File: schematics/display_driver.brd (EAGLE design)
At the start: 100 x 50 mm, 70 parts, among them IC1 TPIC6B595N, IC2 TPIC6B595N, Q1 IRF9530, Q10 BC547A, Q11 IRF9530, Q12 BC547A, Q2 IRF9530, Q3 BC547A, Q4 BC547A, Q5 IRF9530, Q6 BC547A, Q7 IRF9530, Q8 BC547A, Q9 IRF9530

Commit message: schematics: current prototyping status
Working sample :)
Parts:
- removed C_LDP, C_LSDP: (no value), wirepad:1,6/0,9
- removed Q10, Q12, Q3, Q4, Q6, Q8: BC547A, transistor-npn:TO92
- removed R10, R2, R22, R24, R7, R8: 220, resistor:0204/7
- removed R11, R12, R4, R5: 2.2k, resistor:0204/5
- removed R20: 680R, resistor:0207/10
- removed R25, R26: 2.2k, resistor:0207/10
- added BUZZ1: F/BC40, buzzer:F/BC40
- added T1: BC547, transistor:TO92
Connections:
- removed net D7: IC1.17, R20.1
- removed net L_DP: C_LDP.1, C_LSDP.1, R20.2
- removed net N$10: Q7.G, R10.2, R9.1
- removed net N$11: Q8.3, R10.1
- removed net N$13: Q8.2, R4.2
- removed net N$14: Q4.2, R5.2
- removed net N$15: Q6.2, R11.2
- removed net N$16: Q3.2, R12.2
- removed net N$3: Q3.3, R2.1
- removed net N$43: Q9.G, R21.1, R22.2
- removed net N$44: Q10.3, R22.1
- removed net N$45: Q11.G, R23.1, R24.2
- removed net N$46: Q12.3, R24.1
- removed net N$48: Q12.2, R25.2
- removed net N$49: Q10.2, R26.2
- removed net N$5: Q5.G, R6.1, R7.2
- removed net N$6: Q6.3, R7.1
- removed net N$7: Q2.G, R3.1, R8.2
- removed net N$8: Q4.3, R8.1
- new net BUZZ_CTL: CONTROL.6, T1.2
- net +12V: now also BUZZ1.+
- net B_1: now also Q7.G, R9.1; no longer R4.1
- net B_2: now also Q2.G, R3.1; no longer R5.1
- net B_3: now also Q5.G, R6.1; no longer R11.1
- net B_4: now also Q1.G, R1.1; no longer R12.1
- net GND: now also T1.1; no longer Q10.1, Q12.1, Q3.1, Q4.1, Q6.1, Q8.1
- net N$2: now also BUZZ1.-, T1.3; no longer Q1.G, R1.1, R2.2
- net S_1: now also Q11.G, R23.1; no longer R25.1
- net S_2: now also Q9.G, R21.1; no longer R26.1
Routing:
- net BUZZ_CTL: track 0.00 -> 69.2 mm
- net B_3: track 2.54 -> 58.4 mm
- net S_1: track 0.00 -> 55.9 mm
- net GND: track 173.3 -> 118.4 mm, vias 7 -> 6
- net B_4: track 2.54 -> 48.8 mm
- net N$16: track 43.7 -> 0.00 mm
- net N$13: track 42.0 -> 0.00 mm
- net N$14: track 41.1 -> 0.00 mm
- net N$15: track 39.8 -> 0.00 mm
- net B_2: track 2.54 -> 40.2 mm
- net N$48: track 34.9 -> 0.00 mm, vias 1 -> 0
- net B_1: track 2.54 -> 33.0 mm
- net S_2: track 0.00 -> 27.0 mm
- net +12V: track 132.1 -> 156.7 mm
- net N$49: track 14.9 -> 0.00 mm, vias 1 -> 0
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
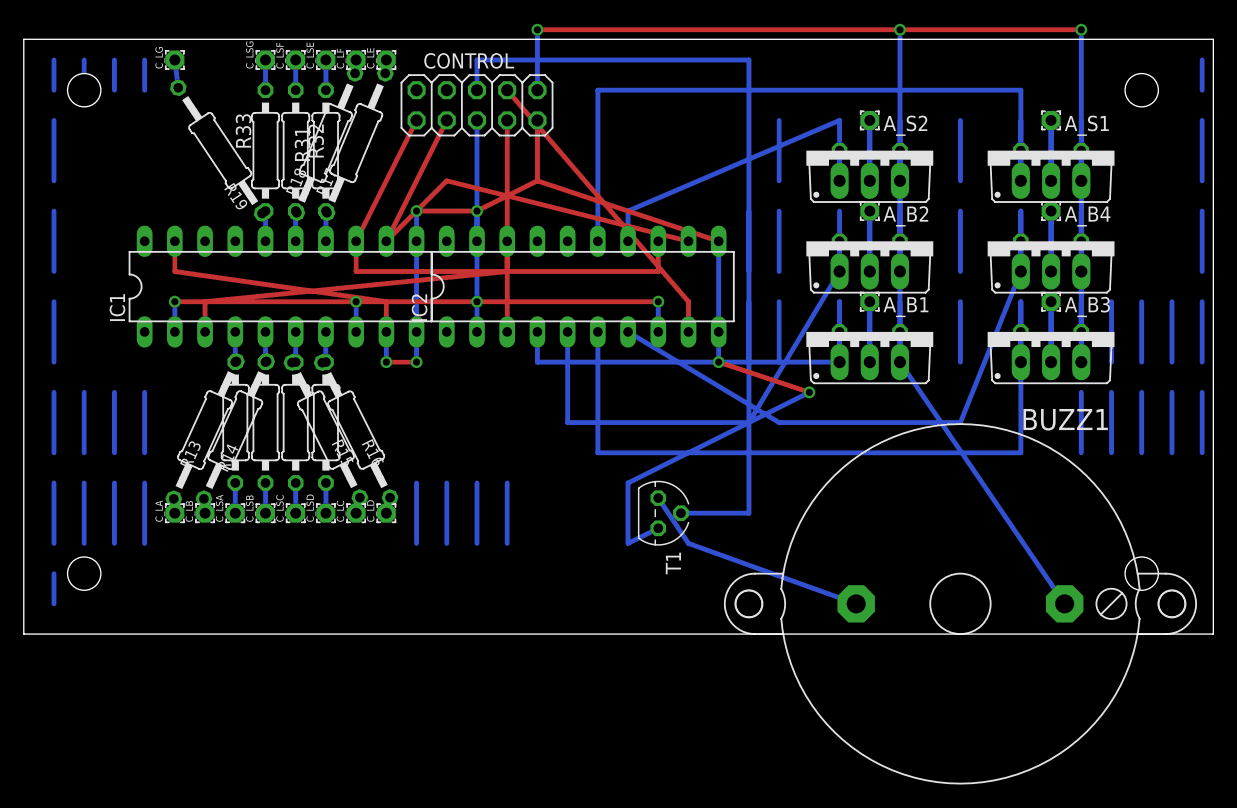
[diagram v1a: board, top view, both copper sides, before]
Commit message: schematics: add correct MOSFET parts, improve redability
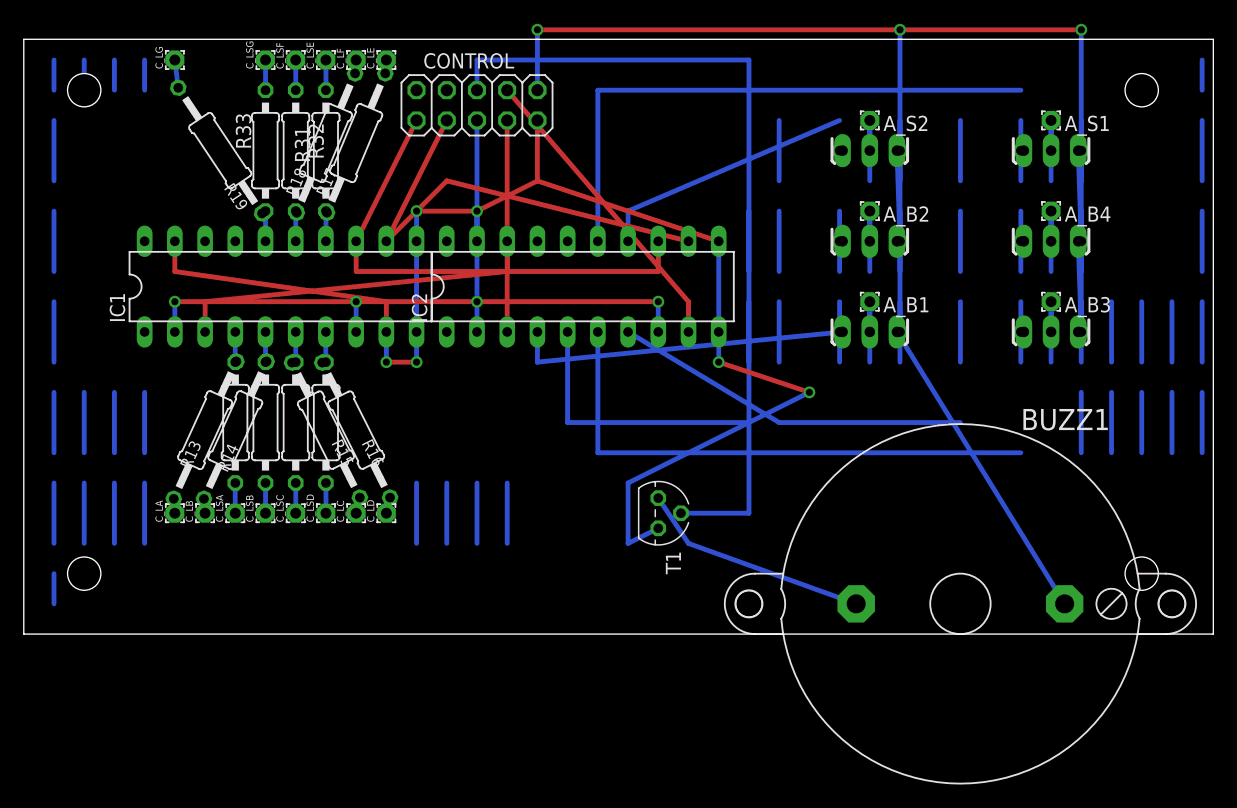
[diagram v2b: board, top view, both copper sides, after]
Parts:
- removed Q11, Q7, Q9: IRF9530, transistor-power:TO220BV
- added Q3, Q4, Q6: IRFU9024V, MINE:TO251AA-V
- Q1, Q2, Q5: value IRF9530 -> IRFU9024V; device transistor-power:TO220BV -> MINE:TO251AA-V
- moved Q1 17.0 mm to (71.1, 25.4)
- moved Q5 15.2 mm to (86.4, 40.6)
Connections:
- net +12V: now also Q1.3, Q2.3, Q3.3, Q4.3, Q5.3, Q6.3; no longer Q1.S, Q11.S, Q2.S, Q5.S, Q7.S, Q9.S
- net B_1: now also Q1.1; no longer Q7.G
- net B_2: now also Q2.1; no longer Q2.G
- net B_3: now also Q3.1; no longer Q5.G
- net B_4: now also Q4.1; no longer Q1.G
- net N$1: now also Q1.2; no longer Q7.D
- net N$12: now also Q4.2; no longer Q1.D
- net N$4: now also Q2.2; no longer Q2.D
- net N$42: now also Q6.2; no longer Q9.D
- net N$47: now also Q5.2; no longer Q11.D
- net N$9: now also Q3.2; no longer Q5.D
- net S_1: now also Q5.1; no longer Q11.G
- net S_2: now also Q6.1; no longer Q9.G
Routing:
- net B_4: track 48.8 -> 30.1 mm
- net B_2: track 40.2 -> 22.9 mm
- net B_3: track 58.4 -> 45.7 mm
- net S_1: track 55.9 -> 48.3 mm
- net S_2: track 27.0 -> 21.9 mm
- net B_1: track 33.0 -> 28.3 mm
- net +12V: track 156.7 -> 152.9 mm
- net N$4: track 5.08 -> 2.54 mm
- net N$12: track 5.08 -> 2.54 mm
- net N$9: track 5.08 -> 2.54 mm
- net N$47: track 5.08 -> 2.54 mm
- net N$42: track 5.08 -> 2.54 mm
- net N$1: track 5.08 -> 2.54 mm

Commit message: schematics: clean up, new design rules
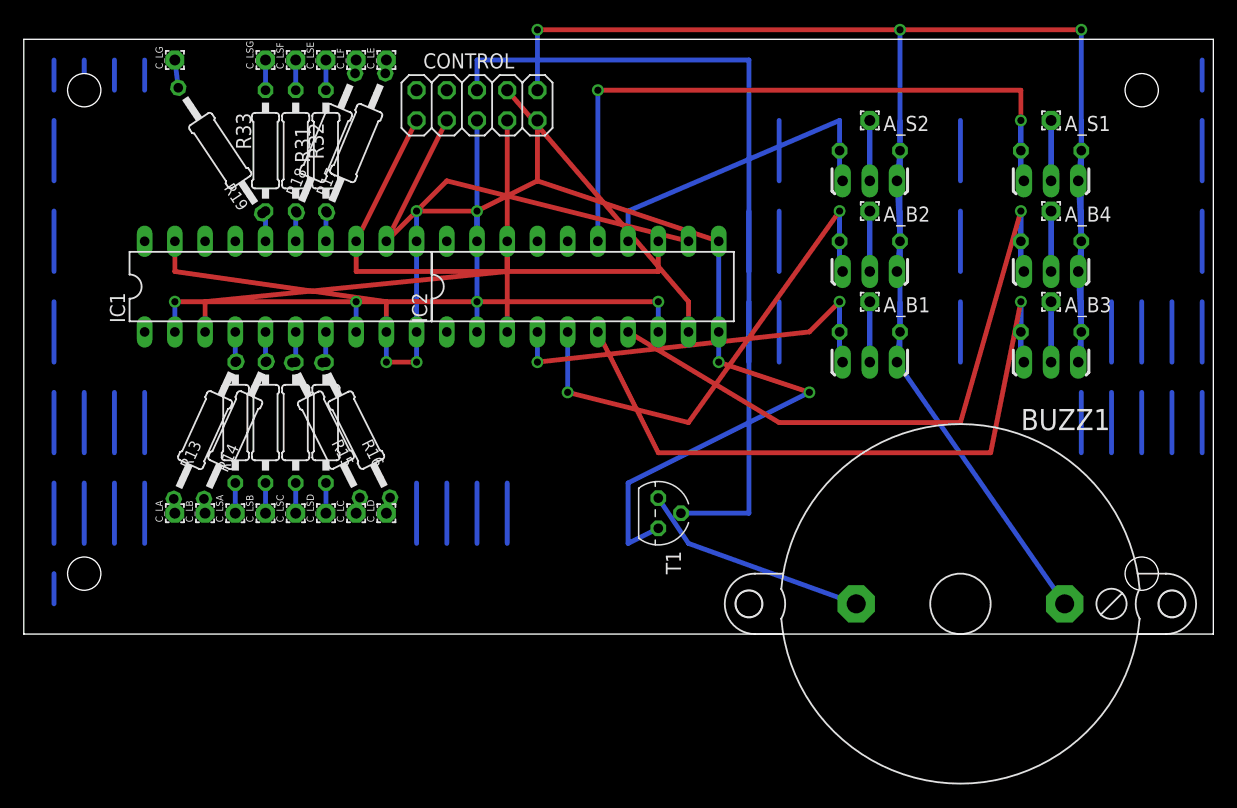
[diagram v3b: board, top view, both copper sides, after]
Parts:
- moved Q2 2.54 mm to (71.1, 30.5)
- moved Q4 2.54 mm to (86.4, 30.5)
- moved Q1 2.54 mm to (71.1, 22.9)
- moved Q3 2.54 mm to (86.4, 22.9)
- moved Q5 2.54 mm to (86.4, 38.1)
- moved Q6 2.54 mm to (71.1, 38.1)
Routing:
- net B_4: track 30.1 -> 53.9 mm, vias 0 -> 1
- net B_2: track 22.9 -> 42.7 mm, vias 0 -> 2
- net B_3: track 45.7 -> 57.6 mm, vias 0 -> 1
- net S_1: track 48.3 -> 56.1 mm, vias 0 -> 2
- net B_1: track 28.3 -> 34.5 mm, vias 0 -> 2
- net S_2: track 21.9 -> 27.2 mm
- net +12V: track 152.9 -> 156.9 mm
- net N$4: track 2.54 -> 5.08 mm
- net N$12: track 2.54 -> 5.08 mm
- net N$9: track 2.54 -> 5.08 mm
- net N$47: track 2.54 -> 5.08 mm
- net N$42: track 2.54 -> 5.08 mm
- net N$1: track 2.54 -> 5.08 mm
